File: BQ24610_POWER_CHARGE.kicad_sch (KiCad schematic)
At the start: 61 parts, among them J1 Screw_Terminal_01x02, J2 Screw_Terminal_01x03, Q1 Si7617DN, Q2 Si7617DN, Q3 SiS412DN, Q4 SiS412DN, Q5 Si7617DN, U1 STN8205A, U2 HY22120-CB, U3 BQ24610

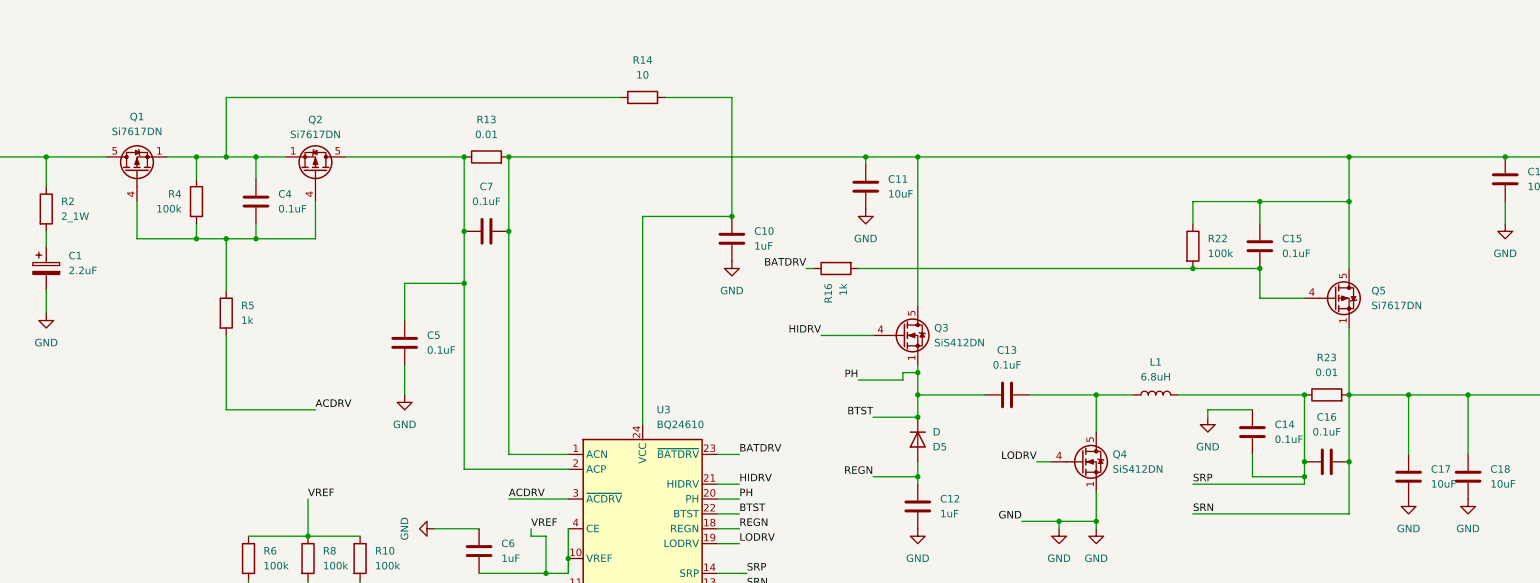
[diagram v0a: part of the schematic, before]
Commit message: Update buck 5-3.8V and change mosfet
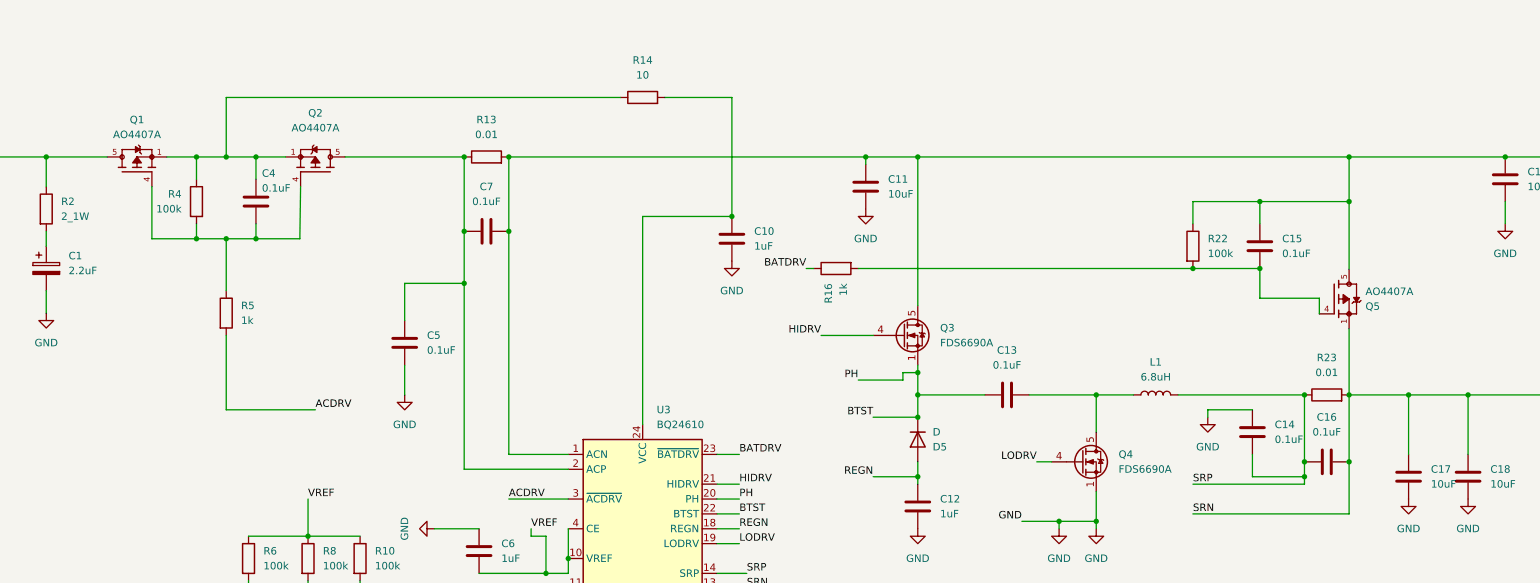
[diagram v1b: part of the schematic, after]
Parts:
- removed Q1, Q2, Q5: Si7617DN, Package_SO:Vishay_PowerPAK_1212-8_Single, symbol Transistor_FET:Si7617DN
- removed Q3, Q4: SiS412DN, Package_SO:Vishay_PowerPAK_1212-8_Single, symbol Transistor_FET:SiS454DN
- added Q1, Q2, Q5: AO4407A, footprintf:SOIC127P600X175-8N, symbol symbol:AO4407A
- added Q3, Q4: FDS6690A, Package_SO:SOIC-8_3.9x4.9mm_P1.27mm, symbol Transistor_FET:FDS6630A
- C1: footprint Capacitor_Tantalum_SMD:CP_EIA-3216-10_Kemet-I_HandSolder -> Capacitor_Tantalum_SMD:CP_EIA-3528-12_Kemet-T_HandSolder
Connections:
- net BTST: now also Q3.1 (S), Q3.2 (S), Q3.3 (S)
- net GND: now also Q4.1 (S), Q4.2 (S), Q4.3 (S)
- net HIDRV: now also Q3.4 (G)
- net LODRV: now also Q4.4 (G)
- net PACK+: now also Q5.1, Q5.2, Q5.3
- net VCC: now also Q1.5, Q1.6, Q1.7, Q1.8
- net VSYSTEM: now also Q3.5 (D), Q3.6 (D), Q3.7 (D), Q3.8 (D), Q5.5, Q5.6, Q5.7, Q5.8
- net at C4.1, R14.1, R4.1: now also Q1.1, Q1.2, Q1.3, Q2.1, Q2.2, Q2.3
- net at C4.2, R4.2, R5.1: now also Q1.4, Q2.4
- net at C5.1, C7.1, R13.1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: now also Q2.5, Q2.6, Q2.7, Q2.8
- net at C15.2, R16.2, R22.2: now also Q5.4
- net at C13.2, L1.1: now also Q4.5 (D), Q4.6 (D), Q4.7 (D), Q4.8 (D)

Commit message: Change POWER_CHARGE
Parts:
- removed C1: 2.2uF, Capacitor_Tantalum_SMD:CP_EIA-3528-12_Kemet-T_HandSolder, symbol Device:C_Polarized
- removed C10, C12: 1uF, Capacitor_SMD:C_0805_2012Metric_Pad1.18x1.45mm_HandSolder, symbol Device:C
- removed C11, C17, C18, C19: 10uF, Capacitor_SMD:C_0805_2012Metric_Pad1.18x1.45mm_HandSolder, symbol Device:C
- removed C13, C14, C15, C16, C9: 0.1uF, Capacitor_SMD:C_0805_2012Metric_Pad1.18x1.45mm_HandSolder, symbol Device:C
- removed C20: 22pF, Capacitor_SMD:C_0805_2012Metric_Pad1.18x1.45mm_HandSolder, symbol Device:C
- removed C8: 0.056uF, Capacitor_SMD:C_0805_2012Metric_Pad1.18x1.45mm_HandSolder, symbol Device:C
- removed D1: SMAJ33A, Diode_SMD:D_SMA, symbol Diode:SMAJ33A
- removed D4: LED, LED_SMD:LED_1206_3216Metric, symbol Device:LED
- removed D5: D, Diode_SMD:D_SMA, symbol Device:D
- removed J1: Screw_Terminal_01x02, TerminalBlock_Phoenix:TerminalBlock_Phoenix_MKDS-3-2-5.08_1x02_P5.08mm_Horizontal, symbol Connector:Screw_Terminal_01x02
- removed Q3, Q4: FDS6690A, Package_SO:SOIC-8_3.9x4.9mm_P1.27mm, symbol Transistor_FET:FDS6630A
- removed Q5: AO4407A, footprintf:SOIC127P600X175-8N, symbol symbol:AO4407A
- removed R11: 14k, Resistor_SMD:R_0805_2012Metric, symbol Device:R
- removed R13, R23: 0.01, Resistor_SMD:R_0805_2012Metric, symbol Device:R
- removed R14: 10, Resistor_SMD:R_0805_2012Metric, symbol Device:R
- removed R15: 100, Resistor_SMD:R_0805_2012Metric, symbol Device:R
- removed R16: 1k, Resistor_SMD:R_0805_2012Metric, symbol Device:R
- removed R17: 9.31k, Resistor_SMD:R_0805_2012Metric, symbol Device:R
- removed R18: 430k, Resistor_SMD:R_0805_2012Metric, symbol Device:R
- removed R19, R20, R21: 10k, Resistor_SMD:R_0805_2012Metric, symbol Device:R
- removed R2: 2_1W, Resistor_SMD:R_0805_2012Metric, symbol Device:R
- removed R22, R25, R8: 100k, Resistor_SMD:R_0805_2012Metric, symbol Device:R
- removed R24: 300k, Resistor_SMD:R_0805_2012Metric, symbol Device:R
- removed U3: BQ24610, Package_DFN_QFN:VQFN-24-1EP_4x4mm_P0.5mm_EP2.45x2.45mm, symbol Battery_Management:BQ24610
- added C3: 10uF, Capacitor_SMD:C_0805_2012Metric_Pad1.18x1.45mm_HandSolder, symbol Device:C
- added D1, D5: B340A, Diode_SMD:D_SMC, symbol Diode:B340
- added D4: BAS40, footprintf:SOT23, symbol symbol:BAS40
- added IC1: LT3650EMSE-8.4_TRPBF, footprintf:SOP65P490X110-13N, symbol symbol:LT3650EMSE-4.2_PBF
- added J2: Screw_Terminal_01x02, TerminalBlock_Phoenix:TerminalBlock_Phoenix_MKDS-3-2-5.08_1x02_P5.08mm_Horizontal, symbol Connector:Screw_Terminal_01x02
- added R3: 0.017, Resistor_SMD:R_0805_2012Metric, symbol Device:R
- added U3: LTC4412xS6, Package_TO_SOT_SMD:TSOT-23-6, symbol Power_Management:LTC4412xS6
- C5: value 0.1uF -> 1uF
- C6: value 1uF -> 10uF
- C7: value 0.1uF -> 100uF
- D2, D3: footprint LED_SMD:LED_1206_3216Metric -> LED_SMD:LED_0805_2012Metric_Pad1.15x1.40mm_HandSolder
- R10: value 100k -> 470k
- R4: value 100k -> 402k
- R5: value 1k -> 47k
- R6: value 100k -> 10k
- R7: value 20k -> 10k
- R9: value 7k -> 0.05
- renumbered C2 to C1, C3 to C2, J2 to J1, R3 to R2, R12 to R8
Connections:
- net ACDRV is gone; now on net GND: R5.2
- net GND: now also C4.2, C6.2, C7.2, C3.2, D5.2 (A), IC1.13 (GND), IC1.6 (TIMER), J2.1 (Pin_1), U3.2 (GND), U3.3 (CTL); no longer C5.2, C6.1, R7.2, R9.2
- net PACK+: now also C6.1, Q1.5, Q1.6, Q1.7, Q1.8, R9.2, D4.1, IC1.9 (BAT), U3.1 (VIN)
- net VCC: now also D1.2 (A), J2.2 (Pin_2); no longer Q1.5, Q1.6, Q1.7, Q1.8
- net VSYSTEM: now also C7.1, Q1.1, Q1.2, Q1.3, Q2.1, Q2.2, Q2.3, R10.1, U3.6 (SENSE); no longer C7.2
- net at R10.2: now also Q2.4, U3.4 (STAT)
- net at R9.1: now also L1.1, IC1.10 (SENSE)
- net at R7.1: now also D3.1 (K); no longer R6.2
- net V_ADAPTER: now reaches Q2.5, Q2.6, Q2.7, Q2.8
- net V_ADAPTER: now also D2.2 (A), D3.2 (A), R4.1, C3.1, IC1.1 (VIN), R3.2; no longer C5.1, C7.1
- net at D2.1 (K): now also R6.1
- net SRP: no longer names the net of L1.2
- net SRP: now also C5.1, D5.1 (K), IC1.12 (SW)
- removed net VREF: C6.2, R10.1, R6.1
- new net: C5.2, D4.3, IC1.11 (BOOST)
- new net: IC1.3 (~{SHDN}), R4.2, R5.1
- new net: Q1.4, U3.5 (GATE)
- new net: C4.1, IC1.7 (RNG/SS)
- new net: IC1.5 (~{FAULT}), R7.2
- new net: IC1.4 (~{CHRG}), R6.2
- new net CLP: D1.1 (K), IC1.2 (CLP), R3.1
- no-connect marks 0 -> 1
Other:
- moved on the sheet: C1, C2, J1, R1, R2, R8, U1, U2

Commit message: CHANGE POWWER _CHARGE
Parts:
- L1: value 6.8uH -> 10uH
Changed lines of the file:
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@@
 		(fields_autoplaced yes)
 		(property "Reference" "L1"
-			(at 193.421 66.6749 0)
+			(at 193.04 66.6749 0)
 			(show_name no)
 			(do_not_autoplace no)
@@
 			)
 		)
-		(property "Value" "6.8uH"
-			(at 193.421 69.2149 0)
+		(property "Value" "10uH"
+			(at 193.04 69.2149 0)
 			(show_name no)
 			(do_not_autoplace no)
